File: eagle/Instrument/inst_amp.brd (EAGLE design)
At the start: 53 x 40.6 mm, 12 parts, among them IC1 INA126U, X1 VCC +/-, X2 Vin, X3 Vout

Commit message: PCB design done
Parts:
- removed LED1: (no value), led:CHIPLED_1206
- added C6, C7: 100nF, rcl:C050-025X075
- added IC2: OP07C, burr-brown:DIL08
- added R4: 360R, rcl:0207/10
- C1, C2: device rcl:C1206 -> rcl:C050-025X075
- C3, C4: value 0,47µF -> 100µF; device rcl:153CLV-0405 -> rcl:E5-10,5
- IC1: value INA126U -> INA126P; device burr-brown:SO08 -> burr-brown:DIL08
- R1: value 18k -> 8k; device resistor:R1206 -> rcl:0207/10
- R2: value 330R -> 180R; device resistor:R1206 -> rcl:0207/10
- R3: value 0R33 -> 0R2; device rcl:VTA55 -> rcl:0414/15
- moved R2 68.2 mm to (73.7, 33.0), turned to 0 degrees
- moved C1 28.5 mm to (48.3, 27.9), turned to 90 degrees
- moved X3 22.5 mm to (50.8, 15.2), turned to 0 degrees
- moved IC1 21.7 mm to (39.4, 24.1)
- moved R1 20.7 mm to (39.4, 33.0)
- moved C3 15.7 mm to (38.1, 8.89)
- moved C2 15.3 mm to (29.2, 20.3), turned to 180 degrees
- moved R3 9.92 mm to (22.9, 27.9), turned to 180 degrees
- moved C4 9.67 mm to (25.4, 8.89), turned to 270 degrees
- moved X1 4.58 mm to (8.89, 8.89)
- moved X2 4.58 mm to (8.89, 25.4)
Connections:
- removed net N$3: C1.1, C4.+, IC1.4, X1.2
- removed net N$8: LED1.A, R2.1
- new net N$4: IC2.3, R2.1, R4.2
- new net REF: IC1.5, IC2.2, IC2.6
- new net V-: C2.1, C3.+, C6.1, IC1.4, IC2.4, R4.1, X1.2
- net GND: now also C6.2, C7.1; no longer LED1.C
- net V+: now also C1.1, C4.+, C7.2, IC2.7; no longer C2.1, C3.+
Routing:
- net V+: track 51.7 -> 157.8 mm
- net V-: track 0.00 -> 105.8 mm
- net N$4: track 0.00 -> 51.3 mm
- net REF: track 0.00 -> 31.1 mm
- net N$3: track 23.7 -> 0.00 mm
- net N$7: track 22.6 -> 33.9 mm
- net N$8: track 7.74 -> 0.00 mm
- net N$5: track 9.08 -> 15.3 mm
- net N$1: track 6.87 -> 5.61 mm
- net N$6: track 30.4 -> 31.1 mm
- removed copper zone on layer 1, net GND
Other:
- board size 53 x 40.6 mm -> 88.6 x 43.2 mm

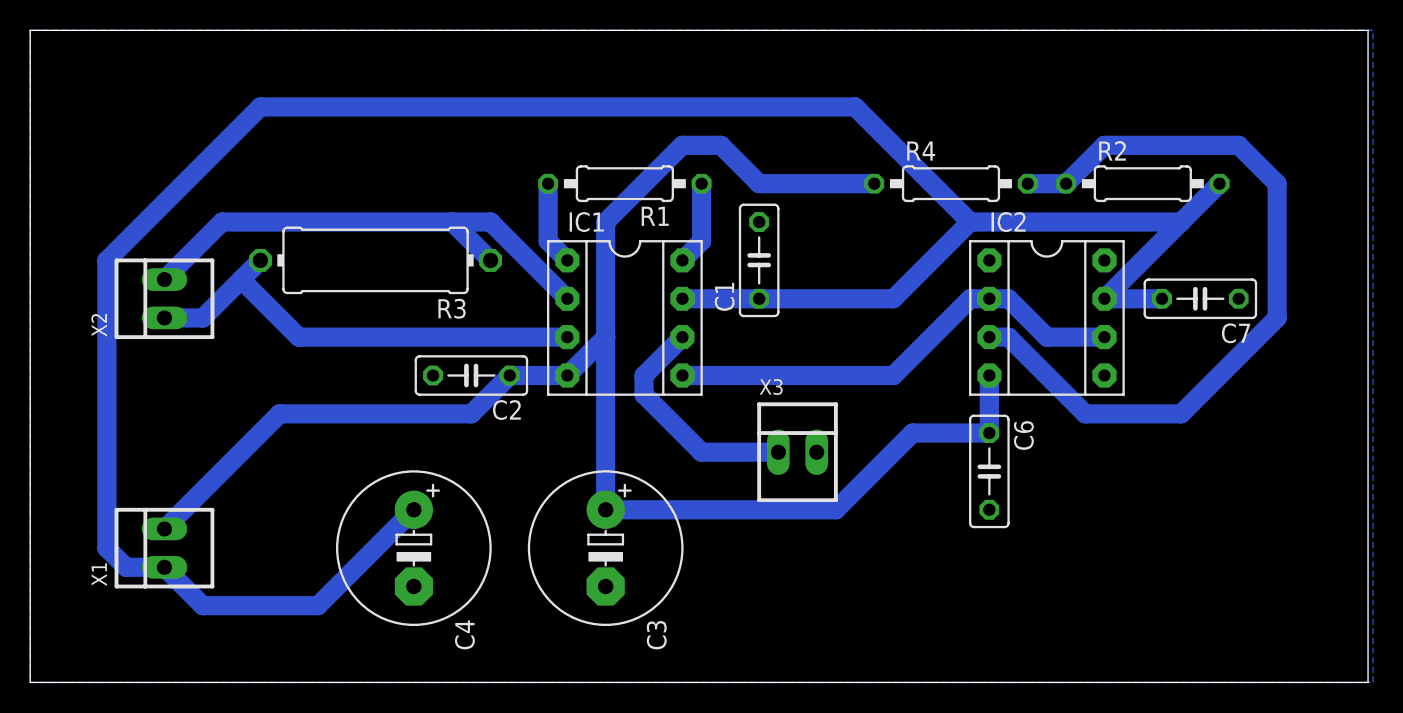
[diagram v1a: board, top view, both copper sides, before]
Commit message: Added lo pass filter
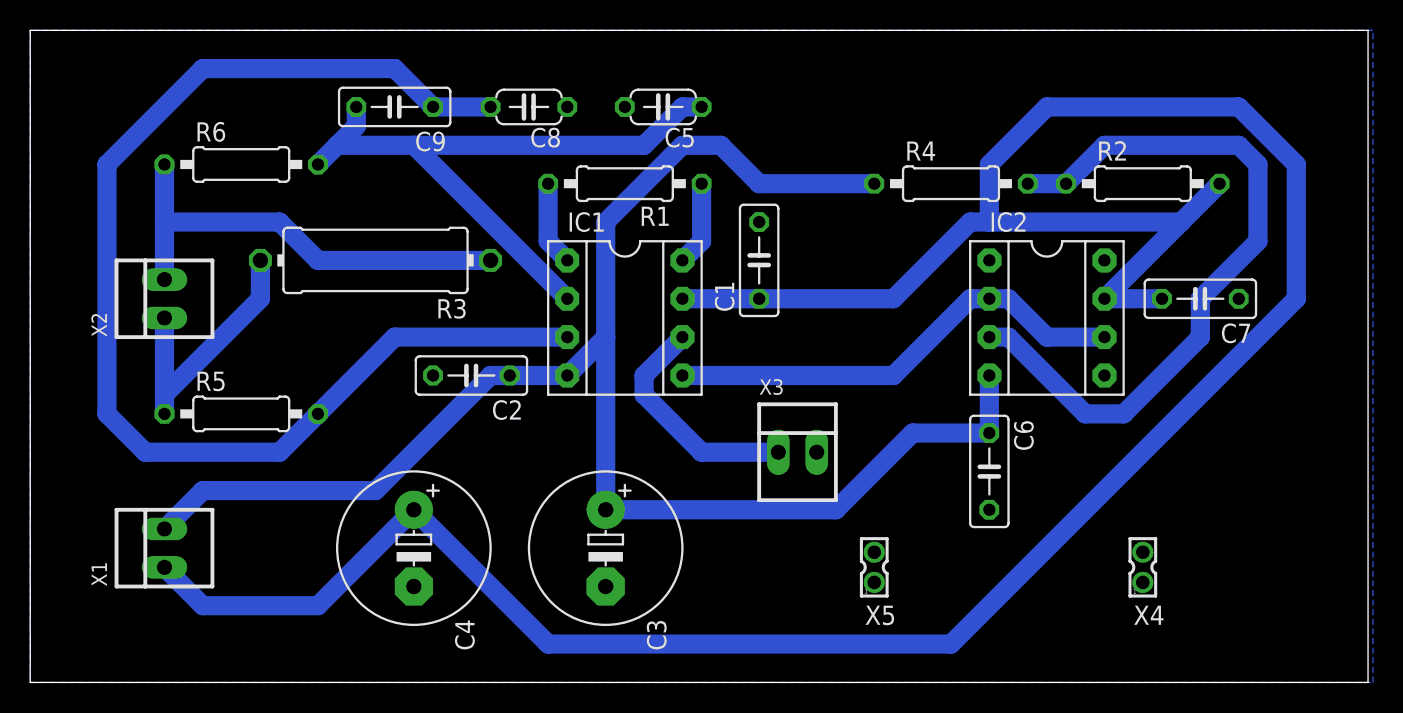
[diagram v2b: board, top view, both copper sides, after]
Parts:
- added C5, C8: 18nF, rcl:C050-024X044
- added C9: 150nF, rcl:C050-025X075
- added R5, R6: 1k, resistor:0207/10
- added X4, X5: 332-02, con-garry:332-02
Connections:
- new net N$3: R3.1, R6.1, X2.2
- new net N$8: R3.2, R5.1, X2.1
- net GND: now also C5.2, C8.1
- net N$6: now also C8.2, C9.1, R5.2; no longer R3.2, X2.1
- net N$7: now also C5.1, C9.2, R6.2; no longer R3.1, X2.2
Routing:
- net N$6: track 31.1 -> 80.3 mm
- net N$3: track 0.00 -> 30.3 mm
- net V+: track 157.8 -> 177.7 mm
- net N$8: track 0.00 -> 17.9 mm
- net N$7: track 33.9 -> 44.4 mm
- net N$4: track 51.3 -> 48.0 mm
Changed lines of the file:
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@@
 <element name="C6" library="rcl" package="C050-025X075" value="100nF" x="63.5" y="13.97" rot="R270"/>
 <element name="C7" library="rcl" package="C050-025X075" value="100nF" x="77.47" y="25.4" rot="R180"/>
+<element name="C5" library="rcl" package="C050-024X044" value="18nF" x="41.91" y="38.1" rot="R180"/>
+<element name="C8" library="rcl" package="C050-024X044" value="18nF" x="33.02" y="38.1" rot="R180"/>
+<element name="C9" library="rcl" package="C050-025X075" value="150nF" x="24.13" y="38.1" rot="R180"/>
+<element name="R5" library="resistor" package="0207/10" value="1k" x="13.97" y="17.78"/>
+<element name="R6" library="resistor" package="0207/10" value="1k" x="13.97" y="34.29"/>
+<element name="X4" library="con-garry" package="332-02" value="332-02" x="73.66" y="7.62"/>
+<element name="X5" library="con-garry" package="332-02" value="332-02" x="55.88" y="7.62"/>
 </elements>
 <signals>
@@
 <contactref element="C7" pad="1"/>
 <contactref element="C6" pad="2"/>
+<contactref element="C8" pad="1"/>
+<contactref element="C5" pad="2"/>
+<wire x1="63.5" y1="11.43" x2="52.07" y2="15.24" width="0" layer="19" extent="1-1"/>
 </signal>
 <signal name="V+">
@@
 <wire x1="57.15" y1="25.4" x2="48.26" y2="25.4" width="1.27" layer="16"/>
 <wire x1="62.23" y1="30.48" x2="57.15" y2="25.4" width="1.27" layer="16"/>
-<wire x1="76.2" y1="30.48" x2="62.23" y2="30.48" width="1.27" layer="16"/>
-<wire x1="6.35" y1="7.62" x2="8.89" y2="7.62" width="1.27" layer="16"/>
-<wire x1="5.08" y1="8.89" x2="6.35" y2="7.62" width="1.27" layer="16"/>
-<wire x1="5.08" y1="27.94" x2="5.08" y2="8.89" width="1.27" layer="16"/>
-<wire x1="15.24" y1="38.1" x2="5.08" y2="27.94" width="1.27" layer="16"/>
-<wire x1="54.61" y1="38.1" x2="15.24" y2="38.1" width="1.27" layer="16"/>
-<wire x1="62.23" y1="30.48" x2="54.61" y2="38.1" width="1.27" layer="16"/>
+<wire x1="76.2" y1="30.48" x2="63.5" y2="30.48" width="1.27" layer="16"/>
+<wire x1="63.5" y1="30.48" x2="62.23" y2="30.48" width="1.27" layer="16"/>
+<wire x1="34.29" y1="2.54" x2="25.4" y2="11.43" width="1.27" layer="16"/>
+<wire x1="60.96" y1="2.54" x2="34.29" y2="2.54" width="1.27" layer="16"/>
+<wire x1="83.82" y1="25.4" x2="60.96" y2="2.54" width="1.27" layer="16"/>
+<wire x1="83.82" y1="34.29" x2="83.82" y2="25.4" width="1.27" layer="16"/>
+<wire x1="80.01" y1="38.1" x2="83.82" y2="34.29" width="1.27" layer="16"/>
+<wire x1="67.31" y1="38.1" x2="80.01" y2="38.1" width="1.27" layer="16"/>
+<wire x1="63.5" y1="34.29" x2="67.31" y2="38.1" width="1.27" layer="16"/>
+<wire x1="63.5" y1="30.48" x2="63.5" y2="34.29" width="1.27" layer="16"/>
 </signal>
 <signal name="N$6">
-<contactref element="X2" pad="1"/>
 <contactref element="IC1" pad="3"/>
-<contactref element="R3" pad="2"/>
-<wire x1="11.43" y1="24.13" x2="8.89" y2="24.13" width="1.27" layer="16"/>
-<wire x1="15.24" y1="27.94" x2="13.97" y2="26.67" width="1.27" layer="16"/>
-<wire x1="13.97" y1="26.67" x2="11.43" y2="24.13" width="1.27" layer="16"/>
-<wire x1="17.78" y1="22.86" x2="35.56" y2="22.86" width="1.27" layer="16"/>
-<wire x1="13.97" y1="26.67" x2="17.78" y2="22.86" width="1.27" layer="16"/>
+<contactref element="C9" pad="1"/>
+<contactref element="C8" pad="2"/>
+<contactref element="R5" pad="2"/>
+<wire x1="30.48" y1="38.1" x2="26.67" y2="38.1" width="1.27" layer="16"/>
+<wire x1="24.13" y1="22.86" x2="19.05" y2="17.78" width="1.27" layer="16"/>
+<wire x1="35.56" y1="22.86" x2="24.13" y2="22.86" width="1.27" layer="16"/>
+<wire x1="24.13" y1="40.64" x2="26.67" y2="38.1" width="1.27" layer="16"/>
+<wire x1="11.43" y1="40.64" x2="24.13" y2="40.64" width="1.27" layer="16"/>
+<wire x1="5.08" y1="34.29" x2="11.43" y2="40.64" width="1.27" layer="16"/>
+<wire x1="5.08" y1="17.78" x2="5.08" y2="34.29" width="1.27" layer="16"/>
+<wire x1="7.62" y1="15.24" x2="5.08" y2="17.78" width="1.27" layer="16"/>
+<wire x1="16.51" y1="15.24" x2="7.62" y2="15.24" width="1.27" layer="16"/>
+<wire x1="19.05" y1="17.78" x2="16.51" y2="15.24" width="1.27" layer="16"/>
 </signal>
 <signal name="N$7">
 <contactref element="IC1" pad="2"/>
-<contactref element="X2" pad="2"/>
-<contactref element="R3" pad="1"/>
-<wire x1="12.7" y1="30.48" x2="8.89" y2="26.67" width="1.27" layer="16"/>
-<wire x1="27.94" y1="30.48" x2="12.7" y2="30.48" width="1.27" layer="16"/>
-<wire x1="30.48" y1="27.94" x2="27.94" y2="30.48" width="1.27" layer="16"/>
-<wire x1="30.48" y1="30.48" x2="35.56" y2="25.4" width="1.27" layer="16"/>
-<wire x1="27.94" y1="30.48" x2="30.48" y2="30.48" width="1.27" layer="16"/>
+<contactref element="C5" pad="1"/>
+<contactref element="C9" pad="2"/>
+<contactref element="R6" pad="2"/>
+<wire x1="21.59" y1="36.83" x2="20.32" y2="35.56" width="1.27" layer="16"/>
+<wire x1="20.32" y1="35.56" x2="19.05" y2="34.29" width="1.27" layer="16"/>
+<wire x1="21.59" y1="38.1" x2="21.59" y2="36.83" width="1.27" layer="16"/>
+<wire x1="43.18" y1="38.1" x2="44.45" y2="38.1" width="1.27" layer="16"/>
+<wire x1="40.64" y1="35.56" x2="43.18" y2="38.1" width="1.27" layer="16"/>
+<wire x1="20.32" y1="35.56" x2="25.4" y2="35.56" width="1.27" layer="16"/>
+<wire x1="25.4" y1="35.56" x2="40.64" y2="35.56" width="1.27" layer="16"/>
+<wire x1="25.4" y1="35.56" x2="35.56" y2="25.4" width="1.27" layer="16"/>
 </signal>
 <signal name="N$5">
@@
 <wire x1="38.1" y1="22.86" x2="38.1" y2="30.48" width="1.27" layer="16"/>
 <wire x1="35.56" y1="20.32" x2="38.1" y2="22.86" width="1.27" layer="16"/>
-<wire x1="16.51" y1="17.78" x2="8.89" y2="10.16" width="1.27" layer="16"/>
-<wire x1="29.21" y1="17.78" x2="16.51" y2="17.78" width="1.27" layer="16"/>
-<wire x1="31.75" y1="20.32" x2="29.21" y2="17.78" width="1.27" layer="16"/>
+<wire x1="11.43" y1="12.7" x2="8.89" y2="10.16" width="1.27" layer="16"/>
+<wire x1="22.86" y1="12.7" x2="11.43" y2="12.7" width="1.27" layer="16"/>
+<wire x1="30.48" y1="20.32" x2="22.86" y2="12.7" width="1.27" layer="16"/>
+<wire x1="31.75" y1="20.32" x2="30.48" y2="20.32" width="1.27" layer="16"/>
 <wire x1="38.1" y1="22.86" x2="38.1" y2="11.43" width="1.27" layer="16"/>
 </signal>
@@
 <wire x1="64.77" y1="22.86" x2="63.5" y2="22.86" width="1.27" layer="16"/>
 <wire x1="69.85" y1="17.78" x2="64.77" y2="22.86" width="1.27" layer="16"/>
-<wire x1="76.2" y1="17.78" x2="69.85" y2="17.78" width="1.27" layer="16"/>
-<wire x1="82.55" y1="24.13" x2="76.2" y2="17.78" width="1.27" layer="16"/>
-<wire x1="82.55" y1="33.02" x2="82.55" y2="24.13" width="1.27" layer="16"/>
-<wire x1="80.01" y1="35.56" x2="82.55" y2="33.02" width="1.27" layer="16"/>
+<wire x1="72.39" y1="17.78" x2="69.85" y2="17.78" width="1.27" layer="16"/>
+<wire x1="77.47" y1="22.86" x2="72.39" y2="17.78" width="1.27" layer="16"/>
+<wire x1="77.47" y1="25.4" x2="77.47" y2="22.86" width="1.27" layer="16"/>
+<wire x1="81.28" y1="29.21" x2="77.47" y2="25.4" width="1.27" layer="16"/>
+<wire x1="81.28" y1="34.29" x2="81.28" y2="29.21" width="1.27" layer="16"/>
+<wire x1="80.01" y1="35.56" x2="81.28" y2="34.29" width="1.27" layer="16"/>
 <wire x1="71.12" y1="35.56" x2="80.01" y2="35.56" width="1.27" layer="16"/>
 <wire x1="68.58" y1="33.02" x2="71.12" y2="35.56" width="1.27" layer="16"/>
 </signal>
+<signal name="N$3">
+<contactref element="X2" pad="2"/>
+<contactref element="R3" pad="1"/>
+<contactref element="R6" pad="1"/>
+<wire x1="8.89" y1="26.67" x2="8.89" y2="30.48" width="1.27" layer="16"/>
+<wire x1="8.89" y1="30.48" x2="8.89" y2="34.29" width="1.27" layer="16"/>
+<wire x1="19.05" y1="27.94" x2="30.48" y2="27.94" width="1.27" layer="16"/>
+<wire x1="16.51" y1="30.48" x2="19.05" y2="27.94" width="1.27" layer="16"/>
+<wire x1="8.89" y1="30.48" x2="16.51" y2="30.48" width="1.27" layer="16"/>
+</signal>
+<signal name="N$8">
+<contactref element="X2" pad="1"/>
+<contactref element="R3" pad="2"/>
+<contactref element="R5" pad="1"/>
+<wire x1="8.89" y1="24.13" x2="8.89" y2="19.05" width="1.27" layer="16"/>
+<wire x1="8.89" y1="19.05" x2="8.89" y2="17.78" width="1.27" layer="16"/>
+<wire x1="15.24" y1="25.4" x2="15.24" y2="27.94" width="1.27" layer="16"/>
+<wire x1="8.89" y1="19.05" x2="15.24" y2="25.4" width="1.27" layer="16"/>
+</signal>
 </signals>

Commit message: Labb4 done
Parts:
- R2: value 180R -> 900R
- R4: value 360R -> 1100R
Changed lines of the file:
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@@
 <attribute name="OC_FARNELL" value="9605304" x="67.31" y="24.13" size="1.778" layer="27" rot="R270" display="off"/>
 </element>
-<element name="R2" library="rcl" package="0207/10" value="180R" x="73.66" y="33.02"/>
-<element name="R4" library="rcl" package="0207/10" value="360R" x="60.96" y="33.02"/>
+<element name="R2" library="rcl" package="0207/10" value="900R" x="73.66" y="33.02"/>
+<element name="R4" library="rcl" package="0207/10" value="1100R" x="60.96" y="33.02"/>
 <element name="C6" library="rcl" package="C050-025X075" value="100nF" x="63.5" y="13.97" rot="R270"/>
 <element name="C7" library="rcl" package="C050-025X075" value="100nF" x="77.47" y="25.4" rot="R180"/>
